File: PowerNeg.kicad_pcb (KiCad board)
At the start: 2 copper layers, 11 parts, among them J1 Conn_01x02_Male, J2 Conn_01x02_Male, U1 MCP3063

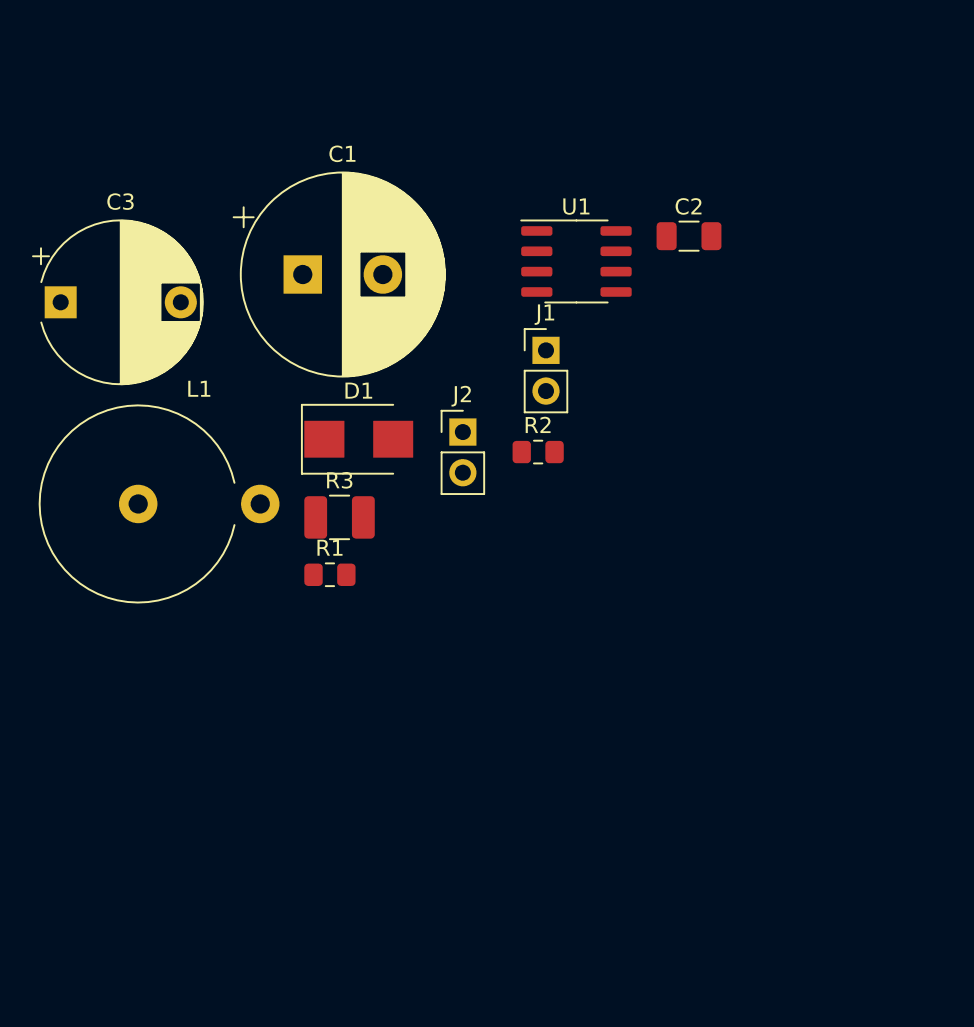
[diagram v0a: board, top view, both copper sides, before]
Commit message: add positiv power source edited PCB
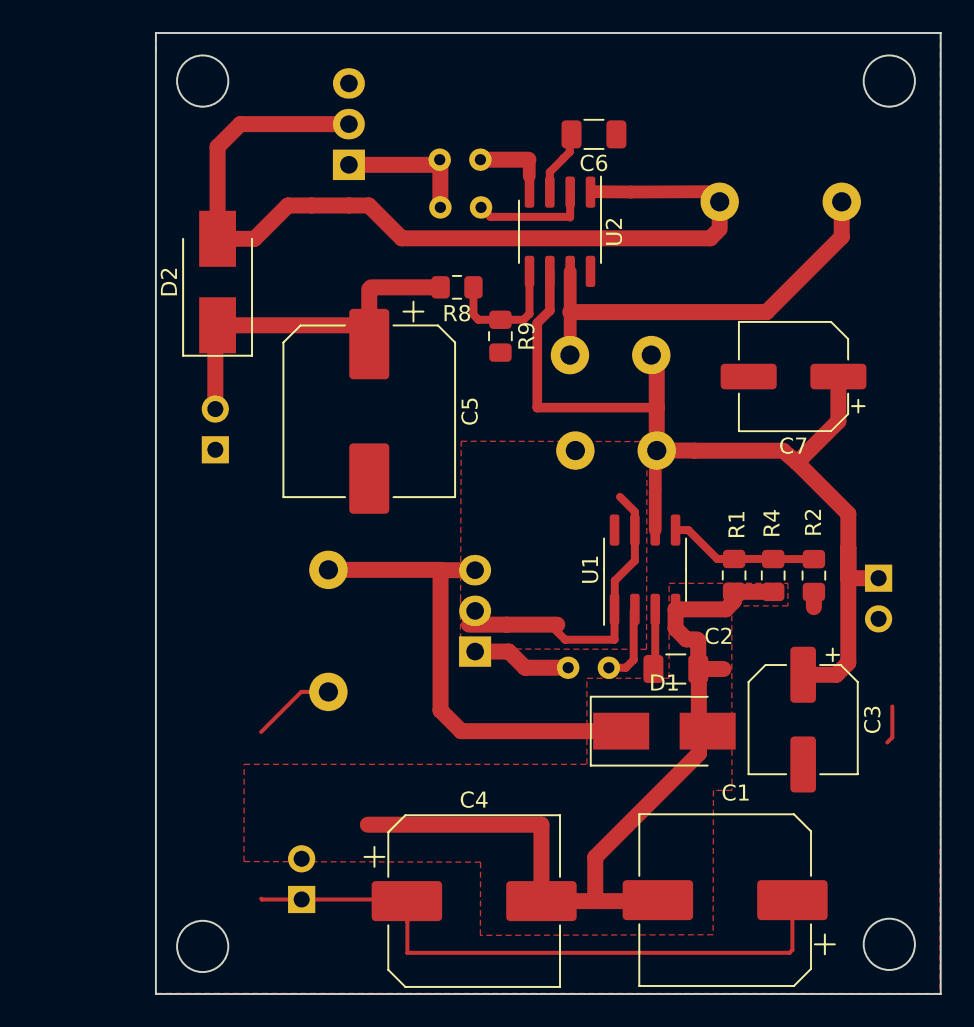
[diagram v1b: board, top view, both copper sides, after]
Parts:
- added C4: 1000 uf, Capacitor_SMD:CP_Elec_10x10.5, F.Cu at (185.9, 104.2)
- added C5: 1000 uf, Capacitor_SMD:CP_Elec_10x10.5, F.Cu at (179.3, 73.6)
- added C6: 2.2 nf, footprint:C_1206, F.Cu at (193.3, 56.3)
- added C7: 100 uf, Capacitor_SMD:CP_Elec_6.3x5.4, F.Cu at (205.8, 71.5)
- added D2: D, Diode_SMD:D_SMB_Handsoldering, F.Cu at (169.8, 65.5)
- added J3: Conn_01x02_Male, Connector_PinHeader_2.54mm:PinHeader_1x02_P2.54mm_Vertical, B.Cu at (169.7, 76.0)
- added L2: L, Inductor_THT:L_Axial_L20.3mm_D12.1mm_P7.62mm_Vertical_Vishay_IHA-101, B.Cu at (201.2, 60.5)
- added Q1: TIP41C, Package_TO_SOT_THT:TO-220-3_Vertical, B.Cu at (185.9, 88.6)
- added Q2: TIP41C, Package_TO_SOT_THT:TO-220-3_Vertical, B.Cu at (178.1, 58.2)
- added R10: 0.24R, Resistor_THT:R_Axial_DIN0516_L15.5mm_D5.0mm_P5.08mm_Vertical, B.Cu at (196.9, 70.1)
- added R4: 20 k, Resistor_SMD:R_0805_2012Metric_Pad1.15x1.40mm_HandSolder, F.Cu at (204.5, 83.9)
- added R5: 1 k, Resistor_THT:R_Axial_DIN0204_L3.6mm_D1.6mm_P2.54mm_Vertical, B.Cu at (194.3, 89.6)
- added R6: 10 k, Resistor_THT:R_Axial_DIN0204_L3.6mm_D1.6mm_P2.54mm_Vertical, B.Cu at (186.3, 57.9)
- added R7: 1 k, Resistor_THT:R_Axial_DIN0204_L3.6mm_D1.6mm_P2.54mm_Vertical, B.Cu at (186.3, 60.9)
- added R8: 47 k, Resistor_SMD:R_0805_2012Metric_Pad1.15x1.40mm_HandSolder, F.Cu at (184.8, 65.9)
- added R9: 22 k, Resistor_SMD:R_0805_2012Metric_Pad1.15x1.40mm_HandSolder, F.Cu at (187.5, 68.9)
- added U2: MCP3063, Package_SO:SOIC-8_3.9x4.9mm_P1.27mm, F.Cu at (191.2, 62.4)
- C1: footprint Capacitor_THT:CP_Radial_D12.5mm_P5.00mm -> Capacitor_SMD:CP_Elec_10x10.5
- C3: footprint Capacitor_THT:CP_Radial_D10.0mm_P7.50mm -> Capacitor_SMD:CP_Elec_6.3x5.4
- D1: footprint Diode_SMD:D_SMB -> Diode_SMD:D_SMB_Handsoldering
- J1, J2, L1: moved to B.Cu
- R1: value 953R -> 1 k
- R3: footprint Resistor_SMD:R_1210_3225Metric_Pad1.42x2.65mm_HandSolder -> Resistor_THT:R_Axial_DIN0516_L15.5mm_D5.0mm_P5.08mm_Vertical; moved to B.Cu
- moved C3 53.2 mm to (206.4, 92.9), turned to 270 degrees
- moved C1 47.1 mm to (201.5, 104.1), turned to 180 degrees
- moved J1 37.5 mm to (175.1, 104.1)
- moved J2 27.5 mm to (211.1, 84.0), turned to 180 degrees
- moved C2 27.0 mm to (198.5, 89.7), turned to 180 degrees
- moved D1 26.4 mm to (197.8, 93.6)
- moved R1 25.2 mm to (202.1, 83.9), turned to 270 degrees
- moved R3 20.2 mm to (197.3, 76.1), turned to 180 degrees
- moved U1 19.7 mm to (196.5, 83.5), turned to 90 degrees
- moved R2 18.9 mm to (207.1, 83.9), turned to 270 degrees
- moved L1 16.7 mm to (176.8, 91.1), turned to 90 degrees
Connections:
- U1 pad 2: Net-(D1-Pad1) -> Net-(R5-Pad1)
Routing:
- net +5V: track 0.00 -> 63.5 mm
- net Net-(D2-Pad2): track 0.00 -> 57.9 mm
- net GND: track 0.00 -> 53.4 mm
- net -9V: track 0.00 -> 53.3 mm
- net Net-(D1-Pad1): track 0.00 -> 30.7 mm
- net Net-(L2-Pad2): track 0.00 -> 26.4 mm
- net +9V: track 0.00 -> 25.8 mm
- net Net-(Q1-Pad2): track 0.00 -> 22.3 mm
- net Net-(R1-Pad1): track 0.00 -> 9.08 mm
- net Net-(Q2-Pad1): track 0.00 -> 8.80 mm
- net Net-(R8-Pad1): track 0.00 -> 8.29 mm
- net Net-(R7-Pad1): track 0.00 -> 7.42 mm
- net Net-(Q1-Pad1): track 0.00 -> 6.53 mm
- net Net-(R5-Pad1): track 0.00 -> 4.94 mm
- net Net-(C6-Pad2): track 0.00 -> 4.08 mm
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- added copper zone on F.Cu, net -9V
- added copper zone on F.Cu, net GND
- added copper zone on F.Cu, net Net-(Q1-Pad2)
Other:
- board outline added: 49 x 60 mm
- board text added: "+9V"
- board text added: "-9V"
- board text added: "IN +5V"
- board text added: "OUT"
